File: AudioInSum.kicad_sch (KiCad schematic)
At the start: 18 parts, among them U7 TLV9062IDR

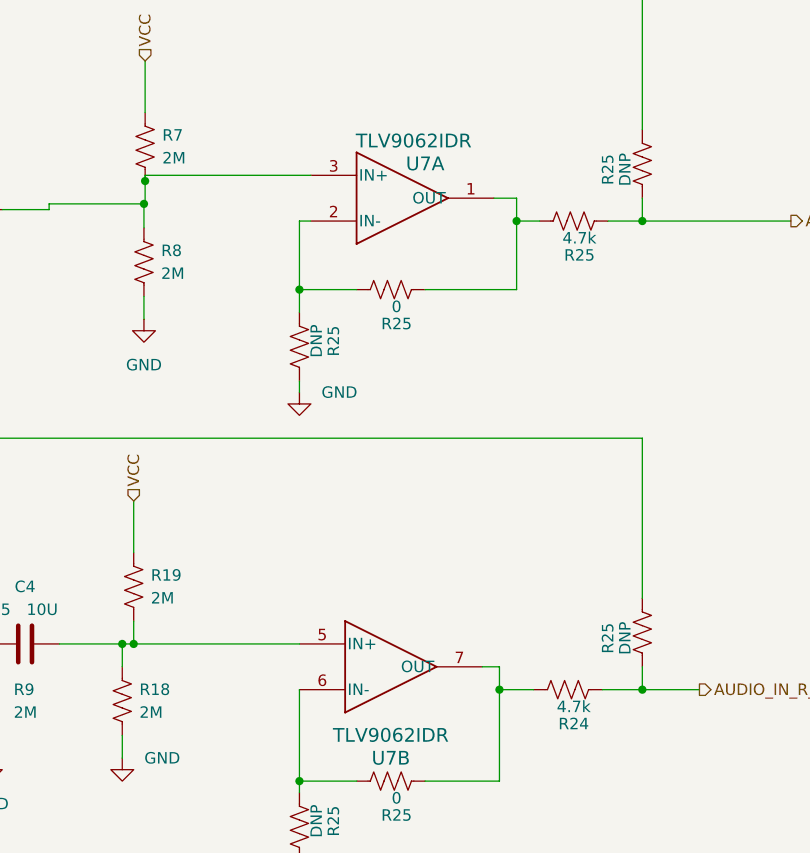
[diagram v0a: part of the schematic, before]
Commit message: PCB cleanup, added accelerometer as easy sensor to begin with
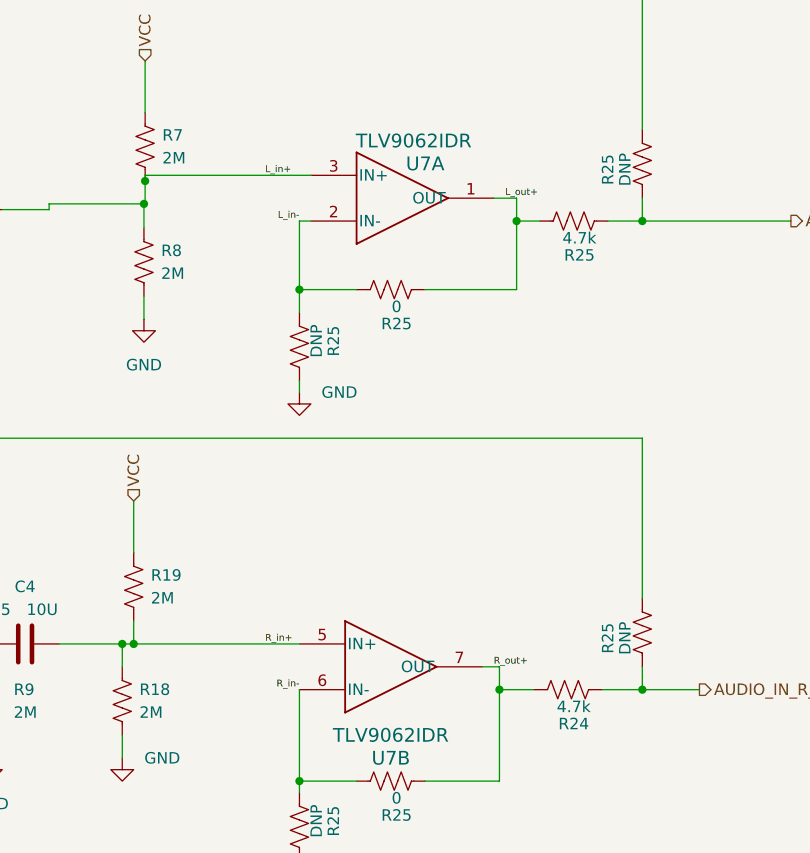
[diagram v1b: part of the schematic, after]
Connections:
- net R_out+: now reaches R24.2, R25.1, U7.7 (OUT)
- net L_out+: now reaches R25.1, R25.2, U7.1 (OUT)
- net L_in-: now reaches R25.1, R25.2, U7.2 (IN-)
- net R_in+: now reaches C4.2, R18.1, R19.2, U7.5 (IN+)
- net L_in+: now reaches C11.2, R7.2, R8.1, U7.3 (IN+)
- net R_in-: now reaches R25.1, R25.2, U7.6 (IN-)
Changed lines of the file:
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@@
   (junction (at 148.59 63.5) (diameter 0) (color 0 0 0 0)
   )
+  (wire (pts (xy 148.59 55.88) (xy 148.59 63.5))
+    (stroke (width 0) (type default))
+  )
+  (wire (pts (xy 120.777 53.975) (xy 131.318 53.975))
+    (stroke (width 0) (type default))
+  )
+  (wire (pts (xy 172.72 55.88) (xy 172.72 63.5))
+    (stroke (width 0) (type default))
+  )
+  (wire (pts (xy 148.59 55.88) (xy 149.86 55.88))
+    (stroke (width 0) (type default))
+  )
+  (wire (pts (xy 182.88 55.88) (xy 186.69 55.88))
+    (stroke (width 0) (type default))
+  )
+  (wire (pts (xy 170.815 107.95) (xy 174.625 107.95))
+    (stroke (width 0) (type default))
+  )
+  (wire (pts (xy 148.59 74.93) (xy 148.59 73.66))
+    (stroke (width 0) (type default))
+  )
+  (wire (pts (xy 131.318 53.975) (xy 131.318 56.642))
+    (stroke (width 0) (type default))
+  )
+  (wire (pts (xy 120.777 54.61) (xy 120.777 53.975))
+    (stroke (width 0) (type default))
+  )
+  (wire (pts (xy 96.52 29.21) (xy 96.52 54.61))
+    (stroke (width 0) (type default))
+  )
+  (wire (pts (xy 131.445 50.8) (xy 131.445 51.435))
+    (stroke (width 0) (type default))
+  )
+  (wire (pts (xy 128.905 102.87) (xy 130.175 102.87))
+    (stroke (width 0) (type default))
+  )
+  (wire (pts (xy 114.3 115.57) (xy 114.3 113.03))
+    (stroke (width 0) (type default))
+  )
+  (wire (pts (xy 148.59 118.11) (xy 154.94 118.11))
+    (stroke (width 0) (type default))
+  )
+  (wire (pts (xy 154.94 63.5) (xy 148.59 63.5))
+    (stroke (width 0) (type default))
+  )
+  (wire (pts (xy 148.59 118.11) (xy 148.59 107.95))
+    (stroke (width 0) (type default))
+  )
+  (wire (pts (xy 182.245 107.95) (xy 186.69 107.95))
+    (stroke (width 0) (type default))
+  )
+  (wire (pts (xy 131.445 50.8) (xy 149.86 50.8))
+    (stroke (width 0) (type default))
+  )
+  (wire (pts (xy 170.815 107.95) (xy 170.815 118.11))
+    (stroke (width 0) (type default))
+  )
+  (wire (pts (xy 186.69 80.01) (xy 105.41 80.01))
+    (stroke (width 0) (type default))
+  )
+  (wire (pts (xy 119.38 180.34) (xy 143.51 180.34))
+    (stroke (width 0) (type default))
+  )
+  (wire (pts (xy 119.38 180.34) (xy 119.38 176.53))
+    (stroke (width 0) (type default))
+  )
+  (wire (pts (xy 131.445 38.1) (xy 131.445 43.815))
+    (stroke (width 0) (type default))
+  )
+  (wire (pts (xy 170.815 118.11) (xy 162.56 118.11))
+    (stroke (width 0) (type default))
+  )
+  (wire (pts (xy 172.72 55.88) (xy 175.26 55.88))
+    (stroke (width 0) (type default))
+  )
+  (wire (pts (xy 186.69 97.79) (xy 186.69 80.01))
+    (stroke (width 0) (type default))
+  )
+  (wire (pts (xy 115.57 54.61) (xy 120.777 54.61))
+    (stroke (width 0) (type default))
+  )
+  (wire (pts (xy 148.59 63.5) (xy 148.59 66.04))
+    (stroke (width 0) (type default))
+  )
+  (wire (pts (xy 143.51 180.34) (xy 143.51 167.64))
+    (stroke (width 0) (type default))
+  )
+  (wire (pts (xy 128.905 102.87) (xy 128.905 105.41))
+    (stroke (width 0) (type default))
+  )
   (wire (pts (xy 130.175 102.87) (xy 148.59 102.87))
     (stroke (width 0) (type default))
   )
-  (wire (pts (xy 120.777 53.975) (xy 131.318 53.975))
-    (stroke (width 0) (type default))
-  )
-  (wire (pts (xy 172.72 55.88) (xy 172.72 63.5))
-    (stroke (width 0) (type default))
-  )
-  (wire (pts (xy 148.59 55.88) (xy 149.86 55.88))
-    (stroke (width 0) (type default))
-  )
-  (wire (pts (xy 182.88 55.88) (xy 186.69 55.88))
-    (stroke (width 0) (type default))
-  )
-  (wire (pts (xy 170.815 107.95) (xy 174.625 107.95))
-    (stroke (width 0) (type default))
-  )
-  (wire (pts (xy 148.59 74.93) (xy 148.59 73.66))
-    (stroke (width 0) (type default))
-  )
-  (wire (pts (xy 131.318 53.975) (xy 131.318 56.642))
-    (stroke (width 0) (type default))
-  )
-  (wire (pts (xy 120.777 54.61) (xy 120.777 53.975))
-    (stroke (width 0) (type default))
-  )
-  (wire (pts (xy 96.52 29.21) (xy 96.52 54.61))
-    (stroke (width 0) (type default))
-  )
-  (wire (pts (xy 131.445 50.8) (xy 131.445 51.435))
-    (stroke (width 0) (type default))
-  )
-  (wire (pts (xy 128.905 102.87) (xy 130.175 102.87))
-    (stroke (width 0) (type default))
-  )
-  (wire (pts (xy 114.3 115.57) (xy 114.3 113.03))
-    (stroke (width 0) (type default))
-  )
-  (wire (pts (xy 148.59 118.11) (xy 154.94 118.11))
-    (stroke (width 0) (type default))
-  )
-  (wire (pts (xy 154.94 63.5) (xy 148.59 63.5))
-    (stroke (width 0) (type default))
-  )
-  (wire (pts (xy 148.59 118.11) (xy 148.59 107.95))
-    (stroke (width 0) (type default))
-  )
-  (wire (pts (xy 182.245 107.95) (xy 186.69 107.95))
-    (stroke (width 0) (type default))
-  )
-  (wire (pts (xy 131.445 50.8) (xy 149.86 50.8))
-    (stroke (width 0) (type default))
-  )
-  (wire (pts (xy 170.815 107.95) (xy 170.815 118.11))
-    (stroke (width 0) (type default))
-  )
-  (wire (pts (xy 186.69 80.01) (xy 105.41 80.01))
-    (stroke (width 0) (type default))
-  )
-  (wire (pts (xy 119.38 180.34) (xy 143.51 180.34))
-    (stroke (width 0) (type default))
-  )
-  (wire (pts (xy 119.38 180.34) (xy 119.38 176.53))
-    (stroke (width 0) (type default))
-  )
-  (wire (pts (xy 131.445 38.1) (xy 131.445 43.815))
-    (stroke (width 0) (type default))
-  )
-  (wire (pts (xy 170.815 118.11) (xy 162.56 118.11))
-    (stroke (width 0) (type default))
-  )
-  (wire (pts (xy 172.72 55.88) (xy 175.26 55.88))
-    (stroke (width 0) (type default))
-  )
-  (wire (pts (xy 186.69 97.79) (xy 186.69 80.01))
-    (stroke (width 0) (type default))
-  )
-  (wire (pts (xy 115.57 54.61) (xy 120.777 54.61))
-    (stroke (width 0) (type default))
-  )
-  (wire (pts (xy 148.59 63.5) (xy 148.59 66.04))
-    (stroke (width 0) (type default))
-  )
-  (wire (pts (xy 143.51 180.34) (xy 143.51 167.64))
-    (stroke (width 0) (type default))
-  )
-  (wire (pts (xy 128.905 102.87) (xy 128.905 105.41))
-    (stroke (width 0) (type default))
-  )
   (wire (pts (xy 172.72 63.5) (xy 162.56 63.5))
     (stroke (width 0) (type default))
@@
   )
   (wire (pts (xy 119.38 184.15) (xy 119.38 180.34))
-    (stroke (width 0) (type default))
-  )
-  (wire (pts (xy 148.59 63.5) (xy 148.59 55.88))
     (stroke (width 0) (type default))
   )
@@
     (effects (font (size 2.27 2.27)) (justify left bottom))
   )
+  (label "L_out+" (at 171.45 53.34 0) (fields_autoplaced)
+    (effects (font (size 0.75 0.75)) (justify left bottom))
+  )
+  (label "L_in-" (at 148.59 55.88 180) (fields_autoplaced)
+    (effects (font (size 0.75 0.75)) (justify right bottom))
+  )
+  (label "R_in-" (at 148.59 107.95 180) (fields_autoplaced)
+    (effects (font (size 0.75 0.75)) (justify right bottom))
+  )
+  (label "L_in+" (at 144.78 50.8 0) (fields_autoplaced)
+    (effects (font (size 0.75 0.75)) (justify left bottom))
+  )
+  (label "R_out+" (at 170.18 105.41 0) (fields_autoplaced)
+    (effects (font (size 0.75 0.75)) (justify left bottom))
+  )
+  (label "R_in+" (at 144.78 102.87 0) (fields_autoplaced)
+    (effects (font (size 0.75 0.75)) (justify left bottom))
+  )
   (hierarchical_label "AUDIO_IN_L_SUMMED" (shape output) (at 203.2 55.88 0) (fields_autoplaced)

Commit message: some cleanup
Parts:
- U7: MnfNumber (none) -> TLV9062IDR
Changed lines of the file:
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@@
       (effects (font (size 1.27 1.27) italic) hide)
+    )
+    (property "MnfNumber" "TLV9062IDR" (at 160.02 53.34 0)
+      (effects (font (size 1.27 1.27)) hide)
     )
     (pin "1")
@@
       (effects (font (size 1.27 1.27) italic) hide)
     )
+    (property "MnfNumber" "TLV9062IDR" (at 158.75 105.41 0)
+      (effects (font (size 1.27 1.27)) hide)
+    )
     (pin "1")
     (pin "2")
@@
       (effects (font (size 1.27 1.27) italic) hide)
     )
-    (pin "1")
+    (property "MnfNumber" "TLV9062IDR" (at 119.38 163.83 0)
+      (effects (font (size 1.27 1.27)) hide)
+    )
+    (pin "1")

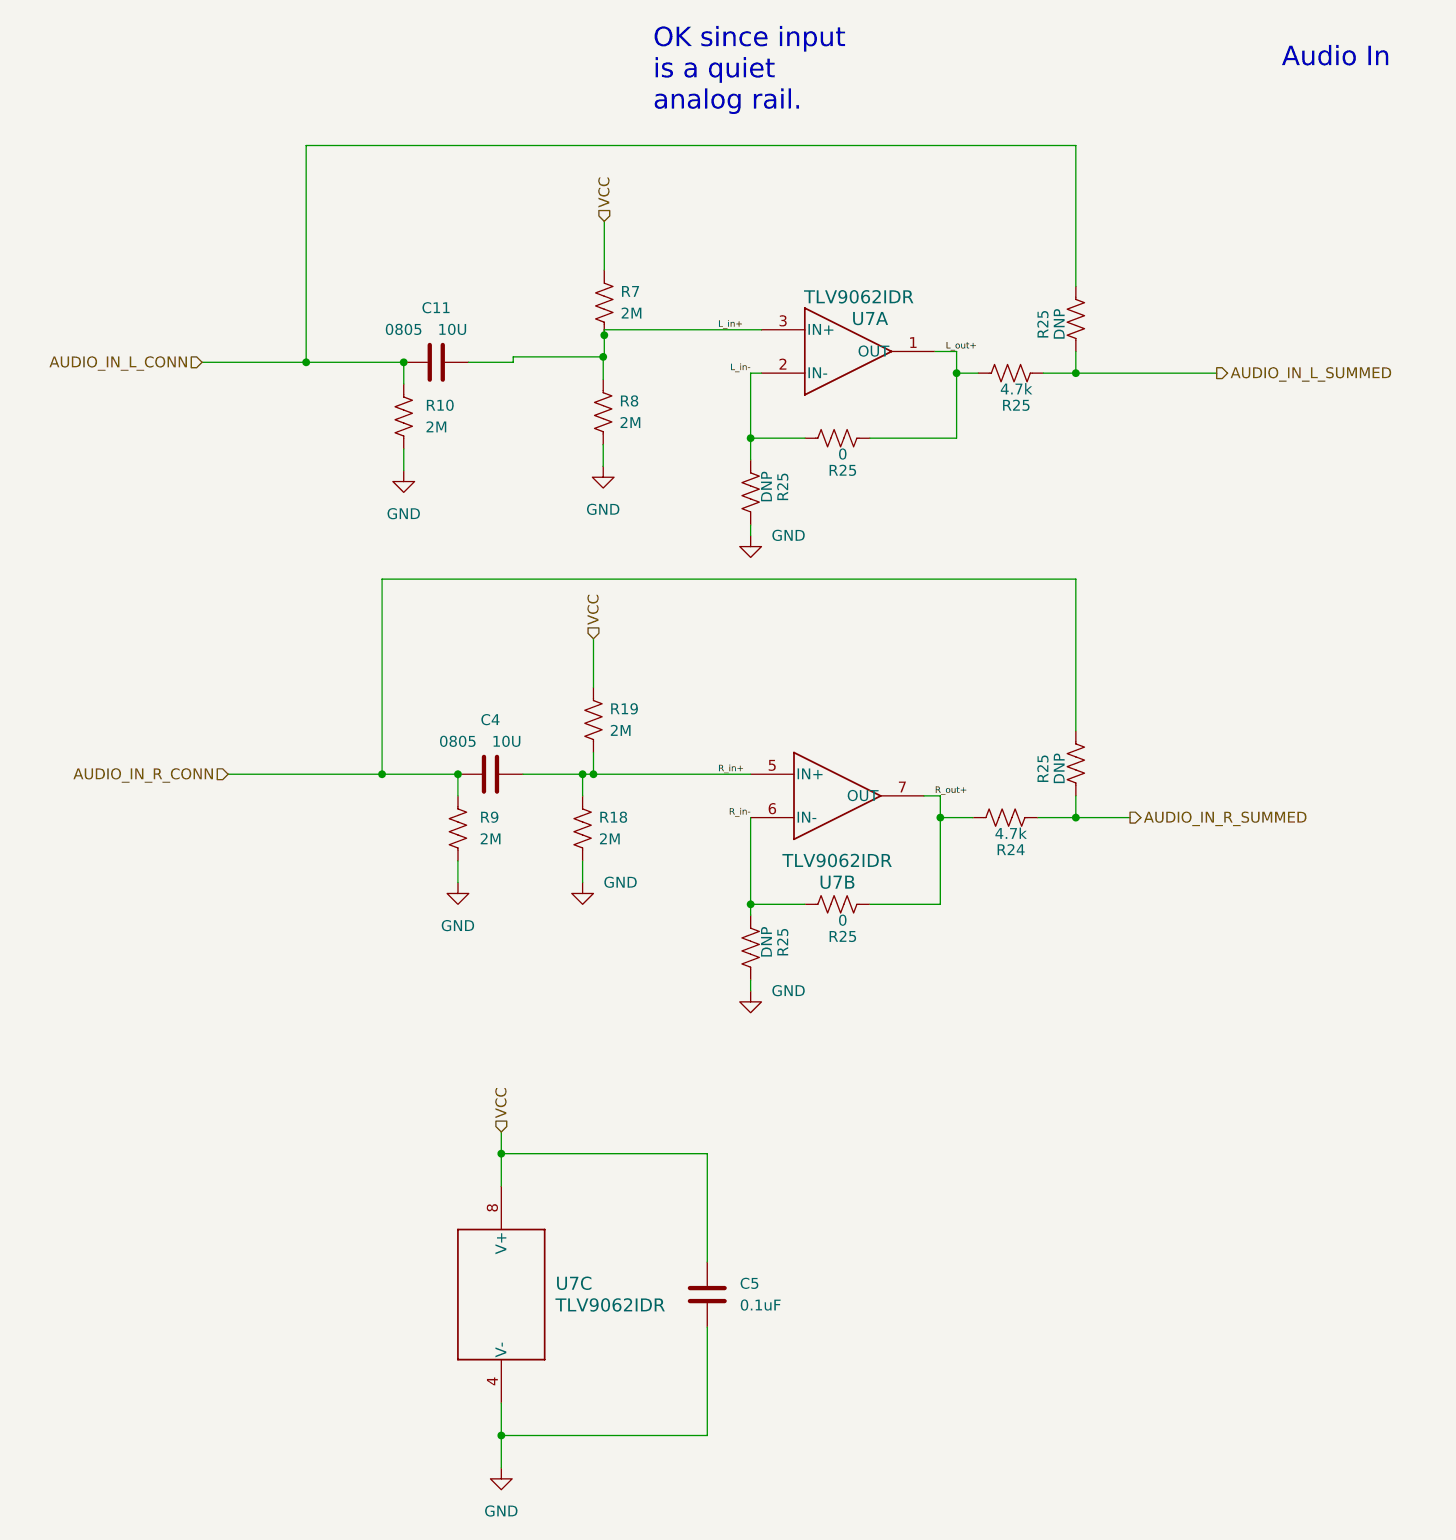
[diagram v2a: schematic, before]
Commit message: updated parts with those available on jlpcb
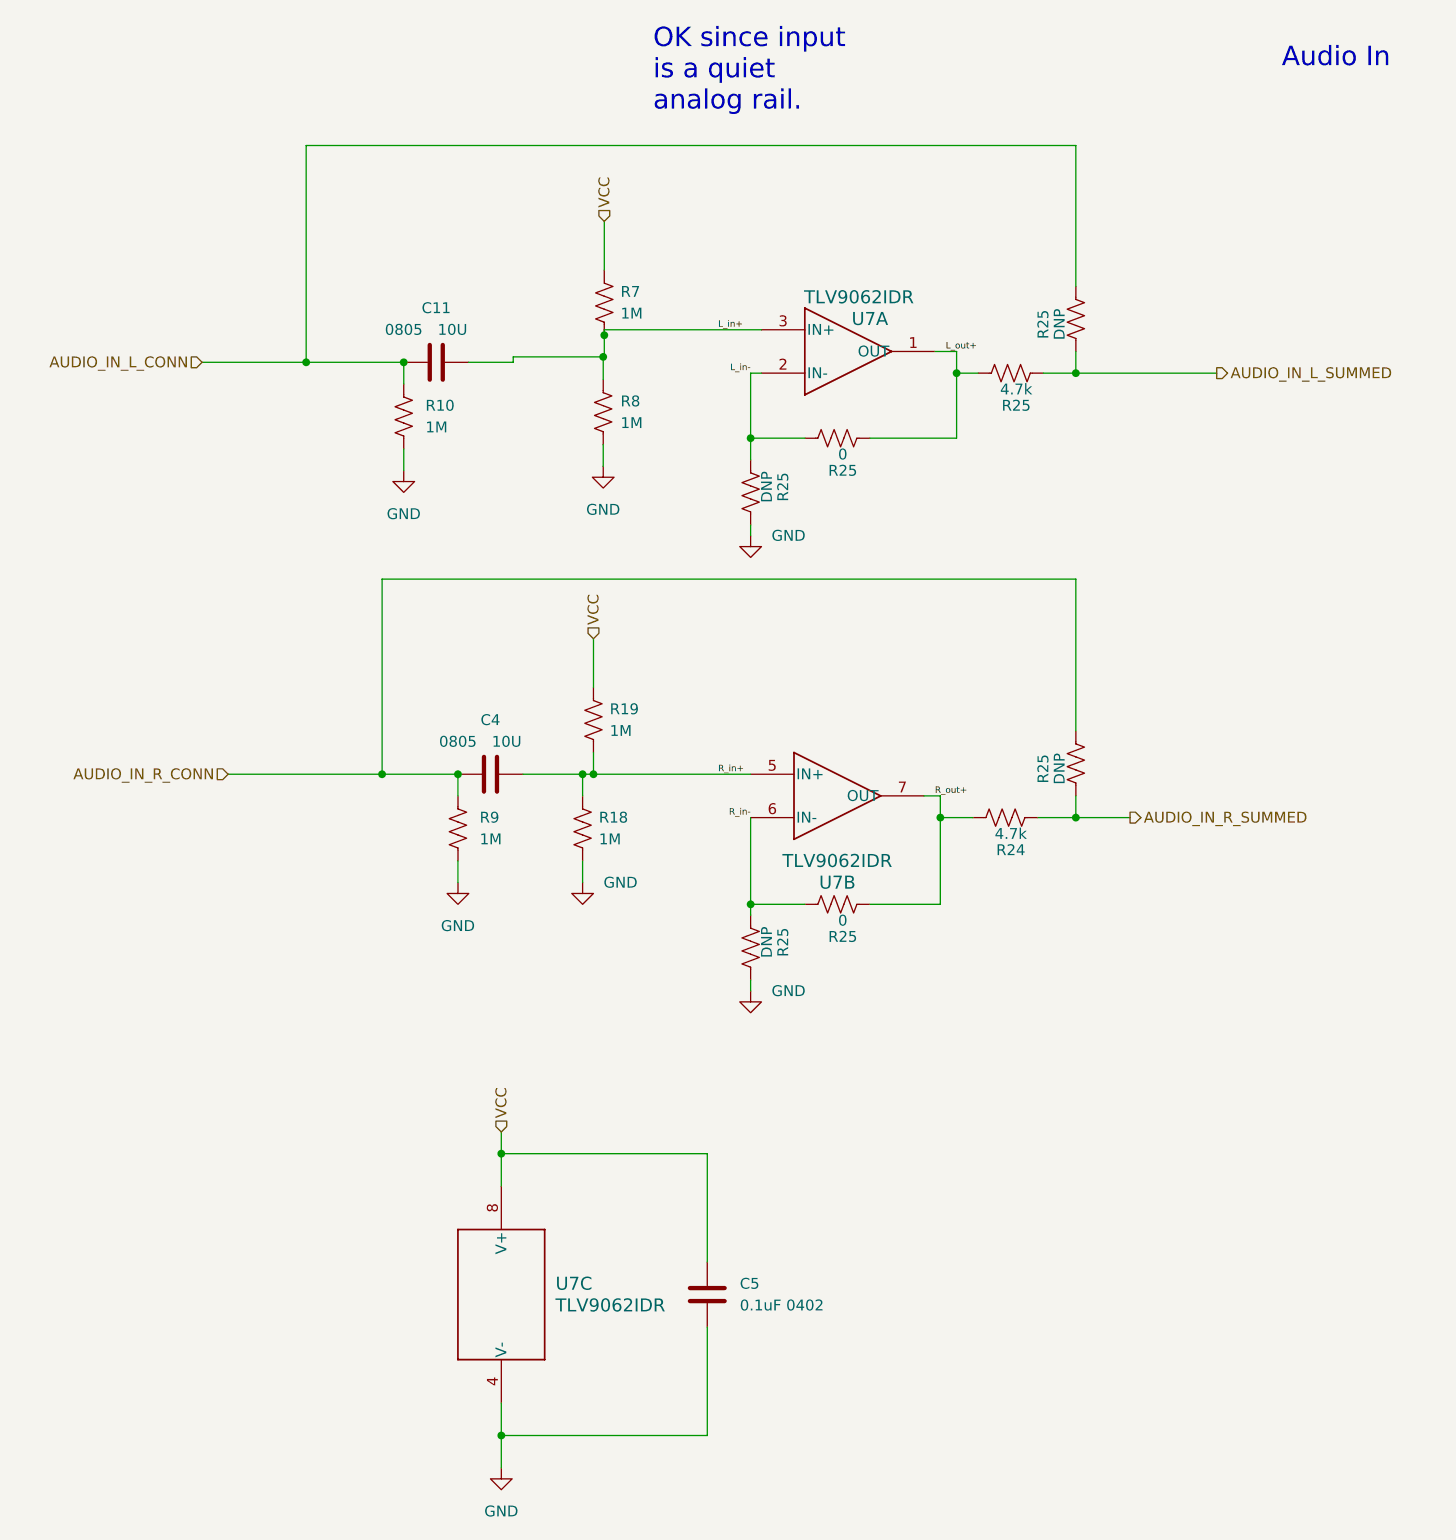
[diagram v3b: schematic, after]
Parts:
- C5: value 0.1uF -> 0.1uF 0402
- R10, R18, R19, R7, R8, R9: value 2M -> 1M
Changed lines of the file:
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@@
       (effects (font (size 1.27 1.27)) (justify left))
     )
-    (property "Value" "2M" (at 110.49 62.23 0)
+    (property "Value" "1M" (at 110.49 62.23 0)
       (effects (font (size 1.27 1.27)) (justify left))
     )
@@
       (effects (font (size 1.27 1.27)) (justify left))
     )
-    (property "Value" "0.1uF" (at 147.32 165.1 0)
+    (property "Value" "0.1uF 0402" (at 147.32 165.1 0)
       (effects (font (size 1.27 1.27)) (justify left))
     )
@@
       (effects (font (size 1.27 1.27)) (justify left))
     )
-    (property "Value" "2M" (at 130.81 110.49 0)
+    (property "Value" "1M" (at 130.81 110.49 0)
       (effects (font (size 1.27 1.27)) (justify left))
     )
@@
       (effects (font (size 1.27 1.27)) (justify left))
     )
-    (property "Value" "2M" (at 132.08 97.79 0)
+    (property "Value" "1M" (at 132.08 97.79 0)
       (effects (font (size 1.27 1.27)) (justify left))
     )
@@
       (effects (font (size 1.27 1.27)) (justify left))
     )
-    (property "Value" "2M" (at 116.84 110.49 0)
+    (property "Value" "1M" (at 116.84 110.49 0)
       (effects (font (size 1.27 1.27)) (justify left))
     )
@@
       (effects (font (size 1.27 1.27)) (justify left))
     )
-    (property "Value" "2M" (at 133.35 48.895 0)
+    (property "Value" "1M" (at 133.35 48.895 0)
       (effects (font (size 1.27 1.27)) (justify left))
     )
@@
   (symbol (lib_id "Device:R_US") (at 131.318 60.452 0) (unit 1)
     (in_bom yes) (on_board yes) (dnp no) (fields_autoplaced)
-    (property "Reference" "R8" (at 133.223 59.182 0)
-      (effects (font (size 1.27 1.27)) (justify left))
-    )
-    (property "Value" "2M" (at 133.223 61.722 0)
-      (effects (font (size 1.27 1.27)) (justify left))
-    )
+    (property "Reference" "R8" (at 133.35 59.182 0)
+      (effects (font (size 1.27 1.27)) (justify left))
+    )
+    (property "Value" "1M" (at 133.35 61.722 0)
+      (effects (font (size 1.27 1.27)) (justify left))
+    )
